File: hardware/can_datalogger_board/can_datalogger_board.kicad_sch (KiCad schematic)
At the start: 12 parts, among them J1 AMP_Superseal_9-6437287-8, U1 RASPBERRY_PI_ZERO_2_W

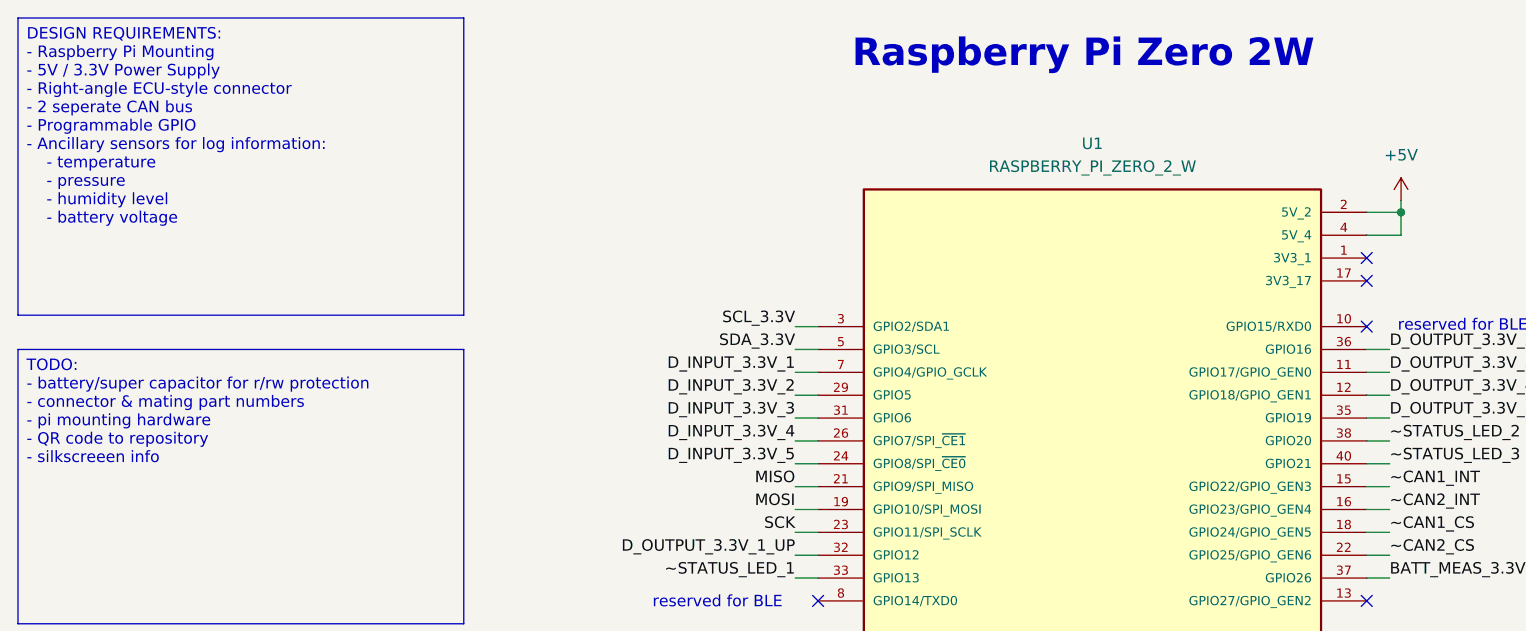
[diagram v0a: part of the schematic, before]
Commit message: PCB component placement
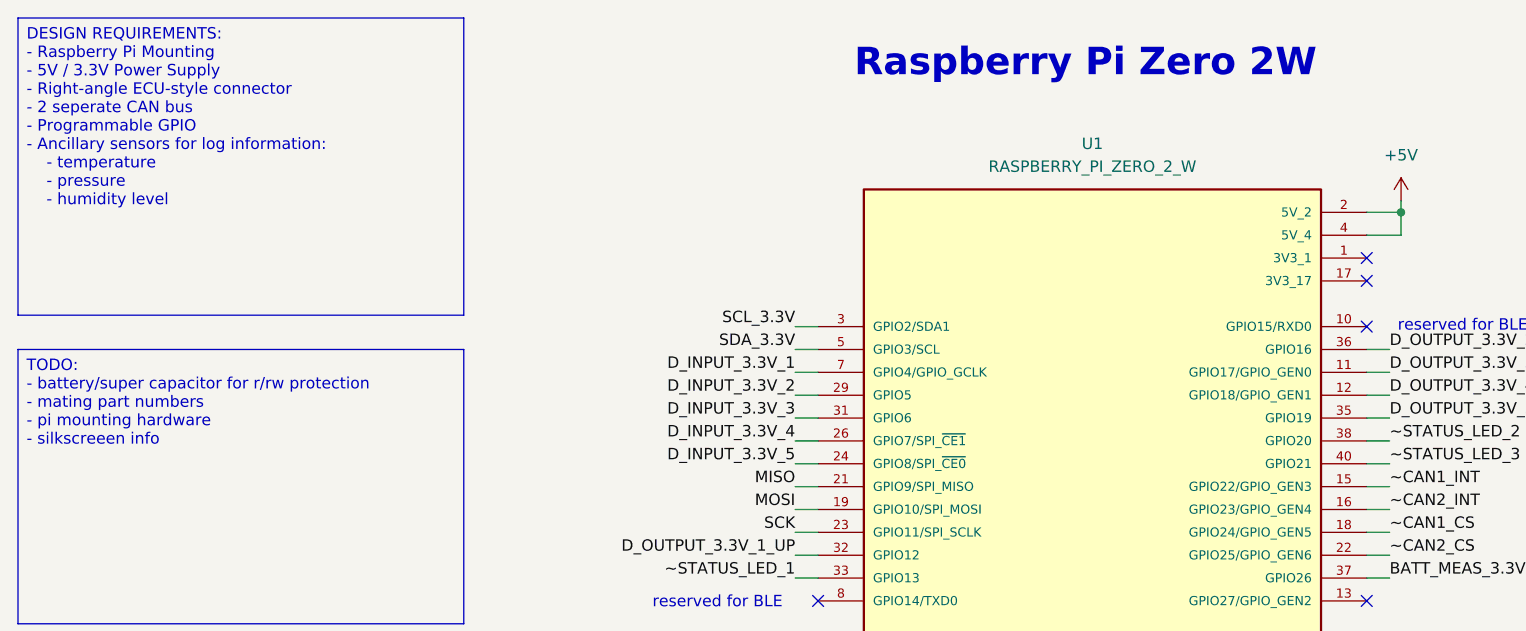
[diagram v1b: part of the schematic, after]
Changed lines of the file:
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@@
 	(text "Raspberry Pi Zero 2W"
 		(exclude_from_sim no)
-		(at 133.604 19.304 0)
+		(at 133.858 20.32 0)
 		(effects
 			(font
@@
 		)
 	)
-	(text_box "TODO:\n- battery/super capacitor for r/rw protection\n- connector & mating part numbers\n- pi mounting hardware\n- QR code to repository\n- silkscreeen info"
+	(text_box "TODO:\n- battery/super capacitor for r/rw protection\n- mating part numbers\n- pi mounting hardware\n- silkscreeen info"
 		(exclude_from_sim no)
 		(at 15.24 52.07 0)
@@
 		)
 	)
-	(text_box "DESIGN REQUIREMENTS:\n- Raspberry Pi Mounting\n- 5V / 3.3V Power Supply\n- Right-angle ECU-style connector\n- 2 seperate CAN bus\n- Programmable GPIO\n- Ancillary sensors for log information:\n	- temperature\n	- pressure\n	- humidity level\n	- battery voltage"
+	(text_box "DESIGN REQUIREMENTS:\n- Raspberry Pi Mounting\n- 5V / 3.3V Power Supply\n- Right-angle ECU-style connector\n- 2 seperate CAN bus\n- Programmable GPIO\n- Ancillary sensors for log information:\n	- temperature\n	- pressure\n	- humidity level"
 		(exclude_from_sim no)
 		(at 15.24 15.24 0)
